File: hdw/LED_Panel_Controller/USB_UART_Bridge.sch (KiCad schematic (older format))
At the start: 46 parts, among them J1501 USB_B_Mini, U1501 74LVC1G97, U1502 CP2105, U1503 TXB0104RGY, U1504 TPD3S014DBVR

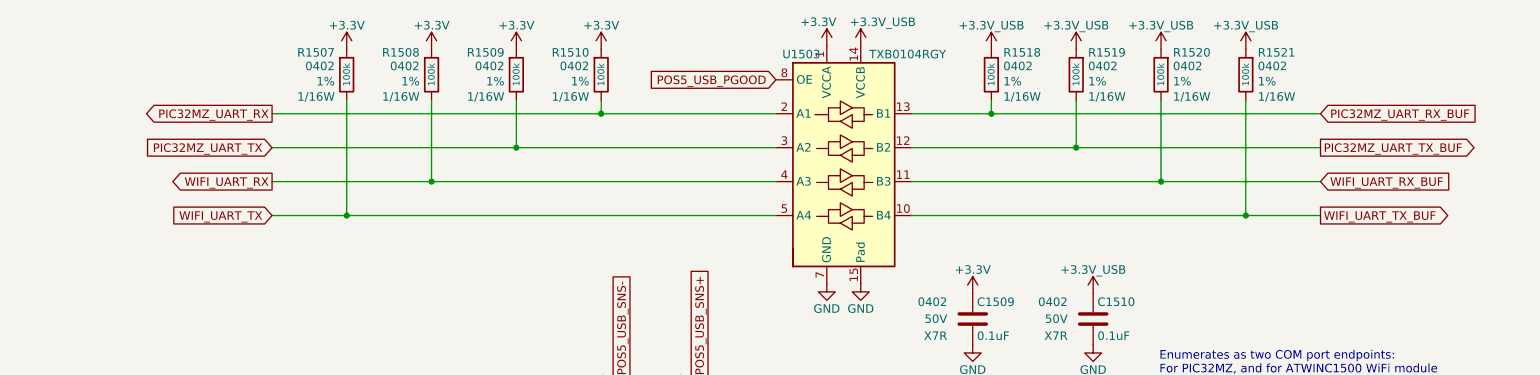
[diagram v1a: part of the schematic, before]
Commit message: USB/power PCB grouping
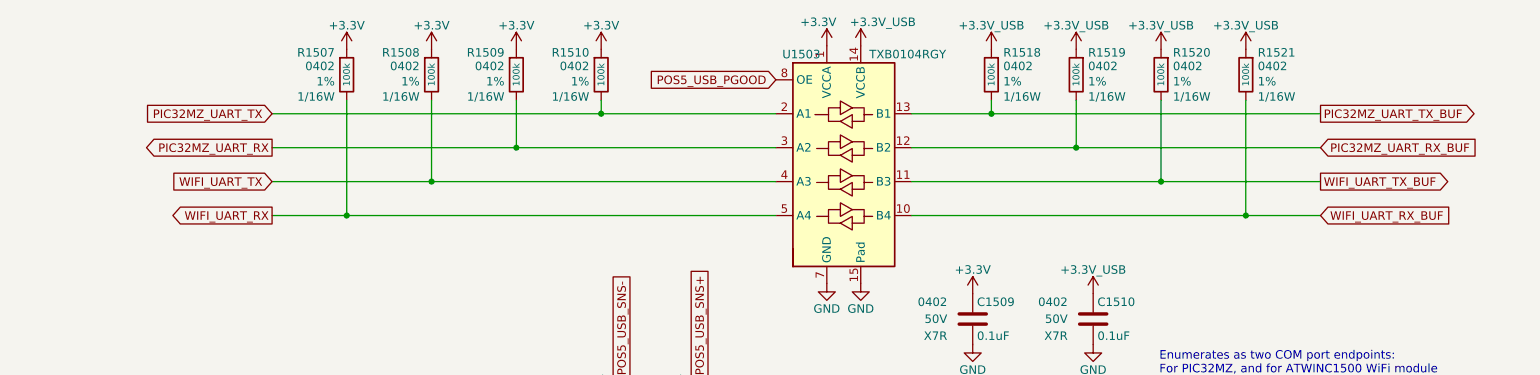
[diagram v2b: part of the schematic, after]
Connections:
- net PIC32MZ_UART_RX: now also R1509.2, U1503.3 (A2); no longer R1510.2, U1503.2 (A1)
- net PIC32MZ_UART_RX_BUF: now also R1519.2, U1503.12 (B2); no longer R1518.2, U1503.13 (B1)
- net PIC32MZ_UART_TX: now also R1510.2, U1503.2 (A1); no longer R1509.2, U1503.3 (A2)
- net PIC32MZ_UART_TX_BUF: now also R1518.2, U1503.13 (B1); no longer R1519.2, U1503.12 (B2)
- net WIFI_UART_RX: now also R1507.2, U1503.5 (A4); no longer R1508.2, U1503.4 (A3)
- net WIFI_UART_RX_BUF: now also R1521.2, U1503.10 (B4); no longer R1520.2, U1503.11 (B3)
- net WIFI_UART_TX: now also R1508.2, U1503.4 (A3); no longer R1507.2, U1503.5 (A4)
- net WIFI_UART_TX_BUF: now also R1520.2, U1503.11 (B3); no longer R1521.2, U1503.10 (B4)
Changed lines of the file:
@@
 Wire Wire Line
 	7790 1550 6820 1550
-Text GLabel 3050 1350 0    50   Output ~ 0
+Text GLabel 3050 1550 0    50   Output ~ 0
 PIC32MZ_UART_RX
-Text GLabel 3050 1550 0    50   Input ~ 0
+Text GLabel 3050 1350 0    50   Input ~ 0
 PIC32MZ_UART_TX
 Text GLabel 6020 1150 0    50   Input ~ 0
@@
 Wire Wire Line
 	8790 1950 9230 1950
-Text GLabel 3050 1750 0    50   Output ~ 0
+Text GLabel 3050 1950 0    50   Output ~ 0
 WIFI_UART_RX
-Text GLabel 3050 1950 0    50   Input ~ 0
+Text GLabel 3050 1750 0    50   Input ~ 0
 WIFI_UART_TX
 $Comp
@@
 Wire Wire Line
 	3490 1950 6020 1950
-Text GLabel 9230 1350 2    50   Input ~ 0
+Text GLabel 9230 1550 2    50   Input ~ 0
 PIC32MZ_UART_RX_BUF
-Text GLabel 9230 1550 2    50   Output ~ 0
+Text GLabel 9230 1350 2    50   Output ~ 0
 PIC32MZ_UART_TX_BUF
-Text GLabel 9230 1750 2    50   Input ~ 0
+Text GLabel 9230 1950 2    50   Input ~ 0
 WIFI_UART_RX_BUF
-Text GLabel 9230 1950 2    50   Output ~ 0
+Text GLabel 9230 1750 2    50   Output ~ 0
 WIFI_UART_TX_BUF
 NoConn ~ 4290 6370

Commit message: having a mid-project crisis
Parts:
- removed C1502, C1503, C1506: 10uF, Capacitors_SMD:C_0402, symbol Custom_Library:C_Custom
- removed C1504: 0.1uF, Capacitors_SMD:C_0402, symbol Custom_Library:C_Custom
- removed D1501: BAT48JFILM, Diode_SMD:D_SOD-323, symbol Diode:BAT48JFILM
- removed D1502, D1504: Green, LEDs:LED_0402, symbol Device:LED
- removed D1503, D1505: Yellow, LEDs:LED_0402, symbol Device:LED
- removed DOC1502: COM_Port_Settings, symbol Custom_Library:COM_Port_Settings
- removed R1505: 1k, Resistors_SMD:R_0402, symbol Custom_Library:R_Custom
- removed R1506, R1517: 10k, Resistors_SMD:R_0402, symbol Custom_Library:R_Custom
- removed R1508, R1509, R1510, R1520, R1521: 100k, Resistors_SMD:R_0402, symbol Custom_Library:R_Custom
- removed R1513, R1514: 0, Resistors_SMD:R_0402, symbol Custom_Library:R_Custom
- removed U1501: 74LVC1G97, Package_TO_SOT_SMD:SOT-363_SC-70-6, symbol Custom_Library:74LVC1G97_Power_BUF
- removed U1502: CP2105, Housings_DFN_QFN:QFN-24-1EP_4x4mm_Pitch0.5mm, symbol Custom_Library:CP2105
- removed U1503: TXB0104RGY, Package_DFN_QFN:Texas_S-PVQFN-N14, symbol Logic_LevelTranslator:TXB0104RGY
- added C1203: 10uF, Capacitors_SMD:C_0402, symbol Custom_Library:C_Custom
- added C1204, C1511: 0.1uF, Capacitors_SMD:C_0402, symbol Custom_Library:C_Custom
- added C1509, C1510: 47pF, Capacitors_SMD:C_0402, symbol Custom_Library:C_Custom
- added D1501: Yellow, LEDs:LED_0402, symbol Device:LED
- added J1502: OSEPP_FTDI_01, Connector_PinHeader_2.54mm:PinHeader_1x06_P2.54mm_Vertical, symbol Connector_Generic:Conn_01x06
- added R1206, R1207: 100k, Resistors_SMD:R_0402, symbol Custom_Library:R_Custom
- added R1210, R1211, R1212, R1218: 0, Resistors_SMD:R_0402, symbol Custom_Library:R_Custom
- added R1215: 10, Resistors_SMD:R_0402, symbol Custom_Library:R_Custom
- added U1501: TLV6700, Package_TO_SOT_SMD:SOT-23-6, symbol Custom_Library:TLV6700
- added U1502: FT234XD, Housings_DFN_QFN:DFN-12-1EP_3x3mm_Pitch0.45mm, symbol Custom_Library:FT234XD
- added U1503: TXB0102DCU, Package_SO:VSSOP-8_2.4x2.1mm_P0.5mm, symbol Logic_LevelTranslator:TXB0102DCU
- C1501: Configuration (none) -> USB; Digi-Key PN 490-10701-1-ND -> 490-10698-1-ND; Voltage 50V -> 25V
- C1502: renamed from C1505; Configuration (none) -> USB; Digi-Key PN 490-10701-1-ND -> 490-10698-1-ND; Voltage 50V -> 25V
- C1505: renamed from C1509; Digi-Key PN 490-10701-1-ND -> 490-10698-1-ND; Voltage 50V -> 25V
- C1506: renamed from C1508; Configuration (none) -> USB; Digi-Key PN 490-10701-1-ND -> 490-10698-1-ND; Voltage 50V -> 25V
- C1507: value 10uF -> 0.1uF; Configuration (none) -> USB; Dielectric X5R -> X7R; Digi-Key PN 1276-1451-1-ND -> 490-10698-1-ND; Voltage 6.3V -> 25V
- C1508: renamed from C1510; Digi-Key PN 490-10701-1-ND -> 490-10698-1-ND; Voltage 50V -> 25V
- DOC1501: Baud_Rate 921600 bps -> 115200 bps
- J1501, L1501, L1502, U1504: Configuration (none) -> USB
- R1501: value 10k -> 1k; Configuration (none) -> USB; Digi-Key PN RMCF0402FT10K0CT-ND -> RMCF0402FT1K00CT-ND
- R1502: value 1k -> 487k; Configuration (none) -> USB; Digi-Key PN RMCF0402FT1K00CT-ND -> RMCF0402FT487KCT-ND
- R1503: value 1k -> 6.04k; Configuration (none) -> USB; Digi-Key PN RMCF0402FT1K00CT-ND -> RMCF0402FT6K04CT-ND
- R1504: value 1k -> 40.2k; Configuration (none) -> USB; Digi-Key PN RMCF0402FT1K00CT-ND -> 311-40.2KLRCT-ND
- R1507: value 100k -> 10k; Configuration (none) -> USB; Digi-Key PN RMCF0402FT100KCT-ND -> RMCF0402FT10K0CT-ND
- R1515: value 0 -> 27; Configuration ~Telemetry -> USB; Digi-Key PN RMCF0402ZT0R00CT-ND -> RMCF0402FT27R0CT-ND
- R1516: value 10 -> 27; Configuration Telemetry -> USB; Digi-Key PN RMCF0402FT10R0CT-ND -> RMCF0402FT27R0CT-ND
- renumbered R1511 to R1208, R1512 to R1209, R1518 to R1216, R1519 to R1217, TP1501 to TP1201
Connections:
- net PIC32MZ_UART_TX_LED is gone; now on an unnamed net: R1504.1
- net WIFI_UART_RX is gone; now on net POS5_USB_PGOOD: R1507.2
- net WIFI_UART_RX_LED is gone; now on an unnamed net: R1503.1
- net WIFI_UART_TX_LED is gone; now on net +5V_USB: R1502.1
- net +3.3V_USB: now also C1507.1, C1511.1, J1502.4 (Pin_4), R1218.2, U1502.3 (3V3OUT), U1502.9 (VCCIO), U1503.7 (VCCB); no longer R1501.1
- net +3V3: now also C1204.1, R1206.1, R1207.1, U1501.5 (Vs), U1503.3 (VCCA)
- net +5V_USB: now also R1501.1, C1203.1, R1210.1, R1211.1, R1212.1, U1502.4 (VCC); no longer R1515.1
- net CONN_USB+: now also R1515.1, U1504.6 (D1), C1509.1; no longer U1504.5 (D2)
- net CONN_USB-: now also R1516.1, U1504.5 (D2), C1510.1; no longer U1504.6 (D1)
- net GND: now also R1504.2, C1203.2, C1204.2, C1509.2, C1510.2, C1511.2, J1502.6 (Pin_6), U1501.2 (GND), U1502.13 (GND), U1502.5 (GND), U1503.2 (GND)
- net PIC32MZ_UART_RX: now also R1207.2, U1503.5 (A1)
- net PIC32MZ_UART_RX_BUF: now also R1216.2, U1502.7 (TXD), U1503.8 (B1); no longer R1217.2
- net PIC32MZ_UART_TX: now also R1206.2, U1503.4 (A2)
- net PIC32MZ_UART_TX_BUF: now also R1217.2, U1502.10 (RXD), U1503.1 (B2); no longer R1216.2
- net POS5_USB_PGOOD: now also R1218.1, U1501.1 (OUTA), U1501.6 (OUTB), U1503.6 (OE)
- net POS5_USB_SNS+: now also R1215.1; no longer R1516.1
- net at R1209.2, U1504.4 (OUT): now also R1210.2, R1211.2, R1212.2, R1215.2; no longer R1515.2, R1516.2
- net at R1502.2: now also U1501.3 (+INA)
- net at R1503.2: now also U1501.4 (-INB)
- net at R1501.2: now also D1501.2 (A)
- new net BRIDGE_USB+: R1515.2, U1502.12 (USBDP)
- new net BRIDGE_USB-: R1516.2, U1502.1 (USBDM)
- new net USB_UART_RX_BUF: J1502.3 (Pin_3)
- new net USB_UART_TX_BUF: J1502.2 (Pin_2)
- new net ~USB_ACTIVE: D1501.1 (K), U1502.6 (CBUS0)
- no-connect marks 8 -> 6
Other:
- note added: "Note: All components on this sheet have "Configuration" field set to "USB", unless otherwise noted"
- note added: "Note: All components within box appear on all configurations"
- note added: "Note: Plugging in an OSEPP FTDI_01 module\non non-USB configs will drive +3.3V onto \n+3.3V_USB net, and force POS5_USB_PGOOD\nhigh in order to enable UART buffer. Module\nVCCIO must be set to +3.3V. This allows a serial\nconnection without any USB components placed\nin the design."
- note removed: "Enumerates as two COM port endpoints:\nFor PIC32MZ, and for ATWINC1500 WiFi module"
- moved on the sheet: C1502, C1505, C1506, C1508, L1501, R1508, R1509, R1510, R1511, TP1501, U1504

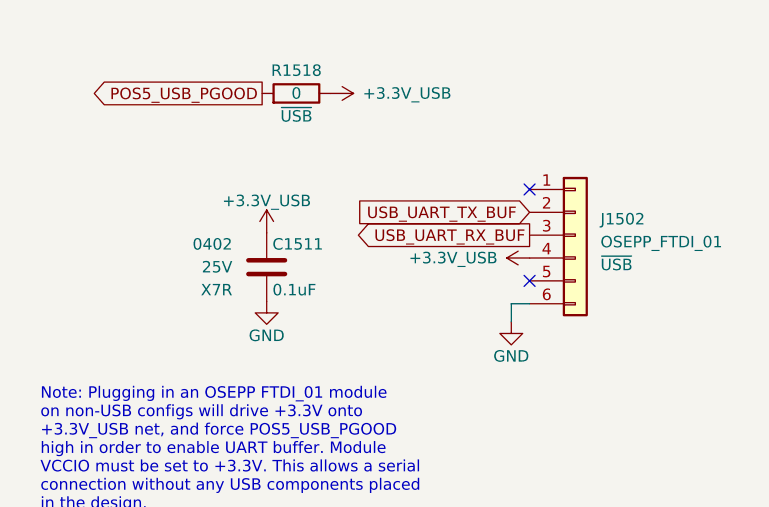
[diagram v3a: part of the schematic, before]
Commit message: reworked schematic to use MLVDS connector instead of wifi module
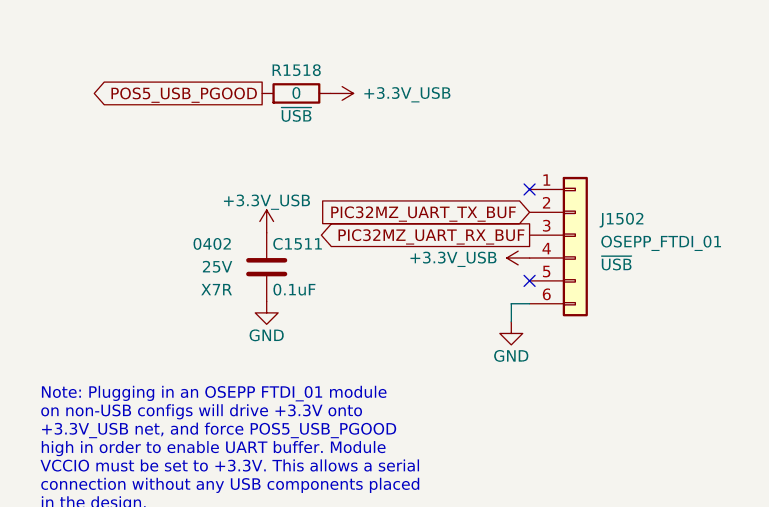
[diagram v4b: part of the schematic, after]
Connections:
- net USB_UART_RX_BUF is gone; now on net PIC32MZ_UART_RX_BUF: J1502.3 (Pin_3)
- net USB_UART_TX_BUF is gone; now on net PIC32MZ_UART_TX_BUF: J1502.2 (Pin_2)
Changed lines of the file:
@@
 encoding utf-8
 Sheet 15 34
-Title "Pulse Oximeter"
-Date "2020-12-31"
-Rev "B"
-Comp "Drew Maatman, Nick Mussoline"
+Title "LED Panel Controller"
+Date "2021-05-30"
+Rev "A"
+Comp "Drew Maatman"
 Comment1 ""
 Comment2 ""
@@
 	0    -1   -1   0
 $EndComp
-Text GLabel 9490 1420 0    50   Output ~ 0
-USB_UART_RX_BUF
-Text GLabel 9490 1320 0    50   Input ~ 0
-USB_UART_TX_BUF
 NoConn ~ 9490 1220
 $Comp
@@
 Text GLabel 1400 1240 0    50   Output ~ 0
 PIC32MZ_UART_RX
+Text GLabel 9490 1320 0    50   Input ~ 0
+PIC32MZ_UART_TX_BUF
+Text GLabel 9490 1420 0    50   Output ~ 0
+PIC32MZ_UART_RX_BUF
 $EndSCHEMATC

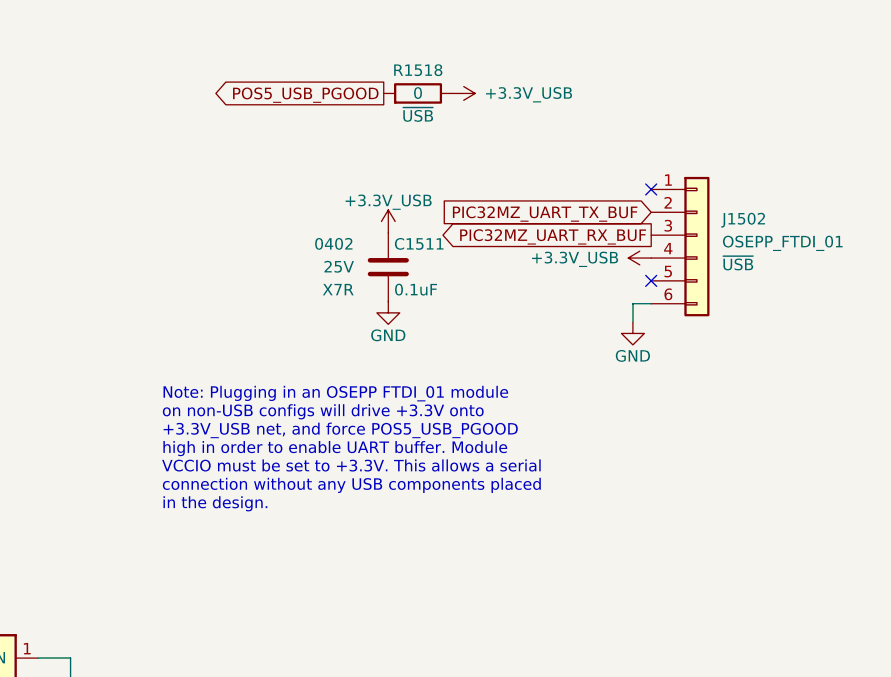
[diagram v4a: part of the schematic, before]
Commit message: arranged more parts on PCB
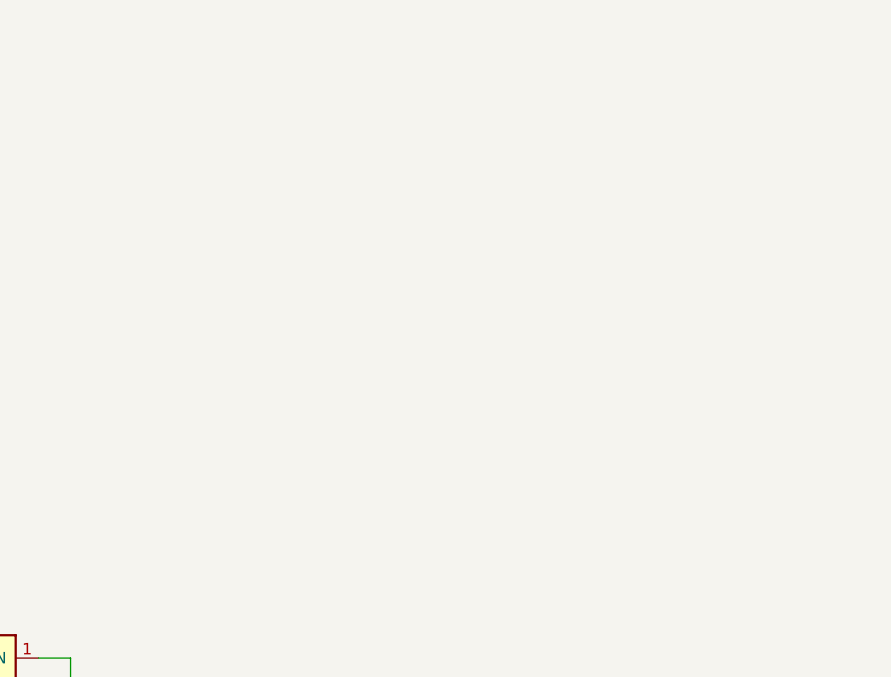
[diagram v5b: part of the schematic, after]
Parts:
- removed C1511: 0.1uF, Capacitors_SMD:C_0402, symbol Custom_Library:C_Custom
- removed J1502: OSEPP_FTDI_01, Connector_PinHeader_2.54mm:PinHeader_1x06_P2.54mm_Vertical, symbol Connector_Generic:Conn_01x06
- removed R1218: 0, Resistors_SMD:R_0402, symbol Custom_Library:R_Custom
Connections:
- no-connect marks 6 -> 4
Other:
- note removed: "Note: Plugging in an OSEPP FTDI_01 module\non non-USB configs will drive +3.3V onto \n+3.3V_USB net, and force POS5_USB_PGOOD\nhigh in order to enable UART buffer. Module\nVCCIO must be set to +3.3V. This allows a serial\nconnection without any USB components placed\nin the design."
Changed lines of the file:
@@
 Wire Wire Line
 	6950 3470 6950 4500
-$Comp
-L Connector_Generic:Conn_01x06 J1502
-U 1 1 5FEF27B0
-P 9690 1420
-F 0 "J1502" H 9800 1490 50  0000 L CNN
-F 1 "OSEPP_FTDI_01" H 9800 1390 50  0000 L CNN
-F 2 "Connector_PinHeader_2.54mm:PinHeader_1x06_P2.54mm_Vertical" H 9690 1420 50  0001 C CNN
-F 3 "~" H 9690 1420 50  0001 C CNN
-F 4 "~USB" H 9800 1290 50  0000 L CNN "Configuration"
-	1    9690 1420
-	1    0    0    -1
-$EndComp
-$Comp
-L power:GND #PWR01541
-U 1 1 5FF04965
-P 9410 1800
-F 0 "#PWR01541" H 9410 1550 50  0001 C CNN
-F 1 "GND" H 9410 1650 50  0000 C CNN
-F 2 "" H 9410 1800 50  0001 C CNN
-F 3 "" H 9410 1800 50  0001 C CNN
-	1    9410 1800
-	1    0    0    -1
-$EndComp
-Wire Wire Line
-	9410 1800 9410 1720
-Wire Wire Line
-	9410 1720 9490 1720
-NoConn ~ 9490 1620
-$Comp
-L Custom_Library:+3.3V_USB #PWR01542
-U 1 1 5FF0AAFA
-P 9490 1520
-F 0 "#PWR01542" H 9490 1370 50  0001 C CNN
-F 1 "+3.3V_USB" V 9490 1660 50  0000 L CNN
-F 2 "" H 9490 1520 50  0001 C CNN
-F 3 "" H 9490 1520 50  0001 C CNN
-	1    9490 1520
-	0    -1   -1   0
-$EndComp
-NoConn ~ 9490 1220
-$Comp
-L Custom_Library:C_Custom C1511
-U 1 1 5FF1CC79
-P 8340 1560
-F 0 "C1511" H 8365 1660 50  0000 L CNN
-F 1 "0.1uF" H 8365 1460 50  0000 L CNN
-F 2 "Capacitors_SMD:C_0402" H 8378 1410 50  0001 C CNN
-F 3 "" H 8365 1660 50  0001 C CNN
-F 4 "0402" H 8190 1660 50  0000 R CNN "display_footprint"
-F 5 "25V" H 8190 1560 50  0000 R CNN "Voltage"
-F 6 "X7R" H 8190 1460 50  0000 R CNN "Dielectric"
-F 7 "490-10698-1-ND" H 8340 1560 50  0001 C CNN "Digi-Key PN"
-	1    8340 1560
-	1    0    0    -1
-$EndComp
-$Comp
-L power:GND #PWR01538
-U 1 1 5FF1D1ED
-P 8340 1710
-F 0 "#PWR01538" H 8340 1460 50  0001 C CNN
-F 1 "GND" H 8340 1560 50  0000 C CNN
-F 2 "" H 8340 1710 50  0001 C CNN
-F 3 "" H 8340 1710 50  0001 C CNN
-	1    8340 1710
-	1    0    0    -1
-$EndComp
-$Comp
-L Custom_Library:+3.3V_USB #PWR01537
-U 1 1 5FF1D1F7
-P 8340 1410
-F 0 "#PWR01537" H 8340 1260 50  0001 C CNN
-F 1 "+3.3V_USB" H 8340 1550 50  0000 C CNN
-F 2 "" H 8340 1410 50  0001 C CNN
-F 3 "" H 8340 1410 50  0001 C CNN
-	1    8340 1410
-	1    0    0    -1
-$EndComp
 Wire Notes Line
 	6300 470  6300 2360
@@
 Text Notes 630  2250 0    50   ~ 0
 Note: All components within box appear on all configurations
-$Comp
-L Custom_Library:R_Custom R?
-U 1 1 5FF25591
-P 8470 800
-AR Path="/5EAE2EF2/5FF25591" Ref="R?"  Part="1"
-AR Path="/5EAE30C7/5FF25591" Ref="R?"  Part="1"
-AR Path="/5EAE2D8A/5FF25591" Ref="R?"  Part="1"
-AR Path="/5EAE2D66/5FF25591" Ref="R?"  Part="1"
-AR Path="/5EAE2F97/5FF25591" Ref="R1218"  Part="1"
-AR Path="/5F582AA0/5FF25591" Ref="R1518"  Part="1"
-F 0 "R1518" V 8370 800 50  0000 C CNN
-F 1 "0" V 8470 800 50  0000 C CNN
-F 2 "Resistors_SMD:R_0402" H 8470 800 50  0001 C CNN
-F 3 "" H 8470 800 50  0001 C CNN
-F 4 "0402" V 8570 800 50  0001 C CNN "display_footprint"
-F 5 "1%" V 8670 800 50  0001 C CNN "Tolerance"
-F 6 "1/16W" V 8770 800 50  0001 C CNN "Wattage"
-F 7 "~USB" V 8570 800 50  0000 C CNN "Configuration"
-F 8 "2019-RK73Z1ETTPCT-ND" H 8470 800 50  0001 C CNN "Digi-Key PN"
-	1    8470 800
-	0    -1   1    0
-$EndComp
-$Comp
-L Custom_Library:+3.3V_USB #PWR01540
-U 1 1 5FF25AF5
-P 8620 800
-F 0 "#PWR01540" H 8620 650 50  0001 C CNN
-F 1 "+3.3V_USB" V 8620 940 50  0000 L CNN
-F 2 "" H 8620 800 50  0001 C CNN
-F 3 "" H 8620 800 50  0001 C CNN
-	1    8620 800
-	0    1    1    0
-$EndComp
-Text Notes 7350 2630 0    50   ~ 0
-Note: Plugging in an OSEPP FTDI_01 module\non non-USB configs will drive +3.3V onto \n+3.3V_USB net, and force POS5_USB_PGOOD\nhigh in order to enable UART buffer. Module\nVCCIO must be set to +3.3V. This allows a serial\nconnection without any USB components placed\nin the design.
-Text GLabel 8320 800  0    50   Output ~ 0
-POS5_USB_PGOOD
 Text GLabel 3720 6640 2    50   Output ~ 0
 POS5_USB_PGOOD
@@
 Text GLabel 1400 1240 0    50   Output ~ 0
 PIC32MZ_UART_RX
-Text GLabel 9490 1320 0    50   Input ~ 0
-PIC32MZ_UART_TX_BUF
-Text GLabel 9490 1420 0    50   Output ~ 0
-PIC32MZ_UART_RX_BUF
 $EndSCHEMATC
